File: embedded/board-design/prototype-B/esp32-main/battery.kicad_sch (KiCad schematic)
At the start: 14 parts, among them J8 Conn_01x03_Socket, Q5 FDN340P, Q6 FDN340P, U5 LTC4054ES5-4.2

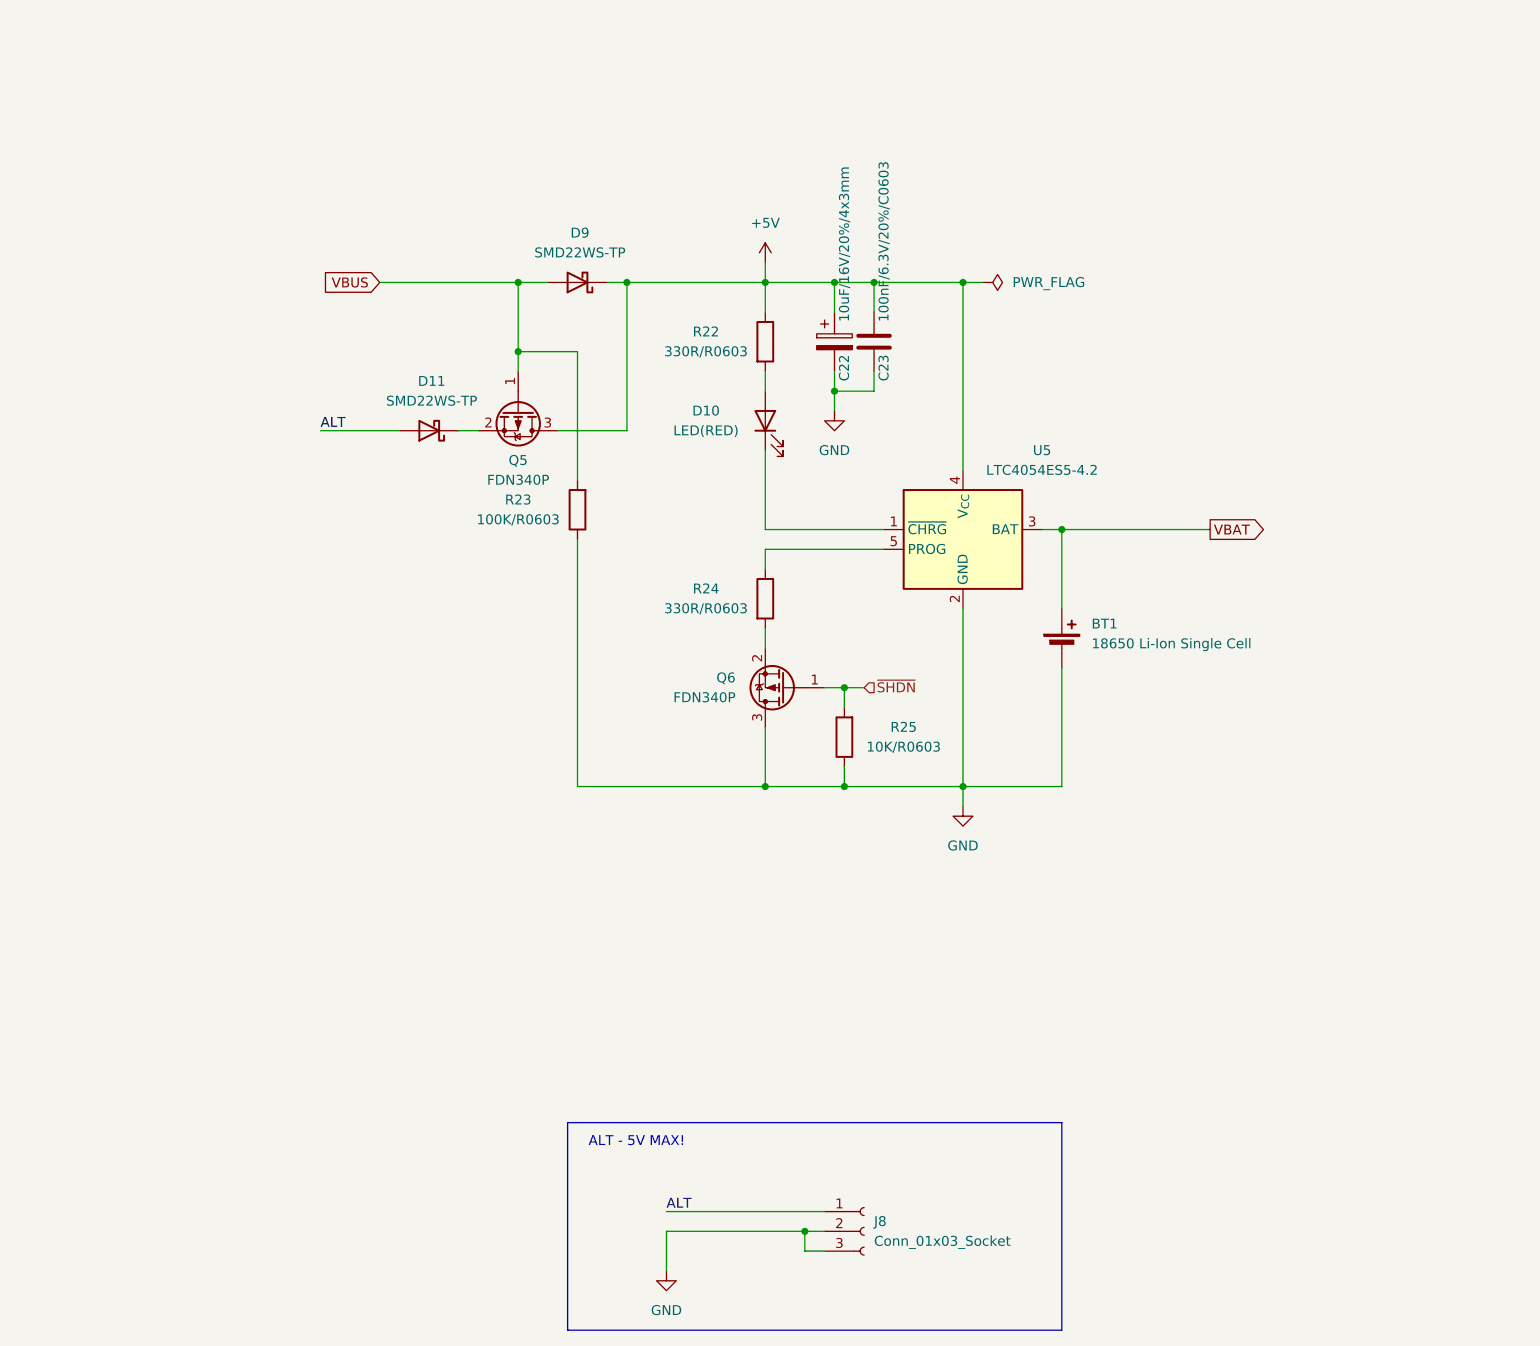
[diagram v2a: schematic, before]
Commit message: [prototype-B]
Refactored power scheme.

Signed-off-by: Nicolae-Andrei Vasile <vasilenicolaeandrei@gmail.com>
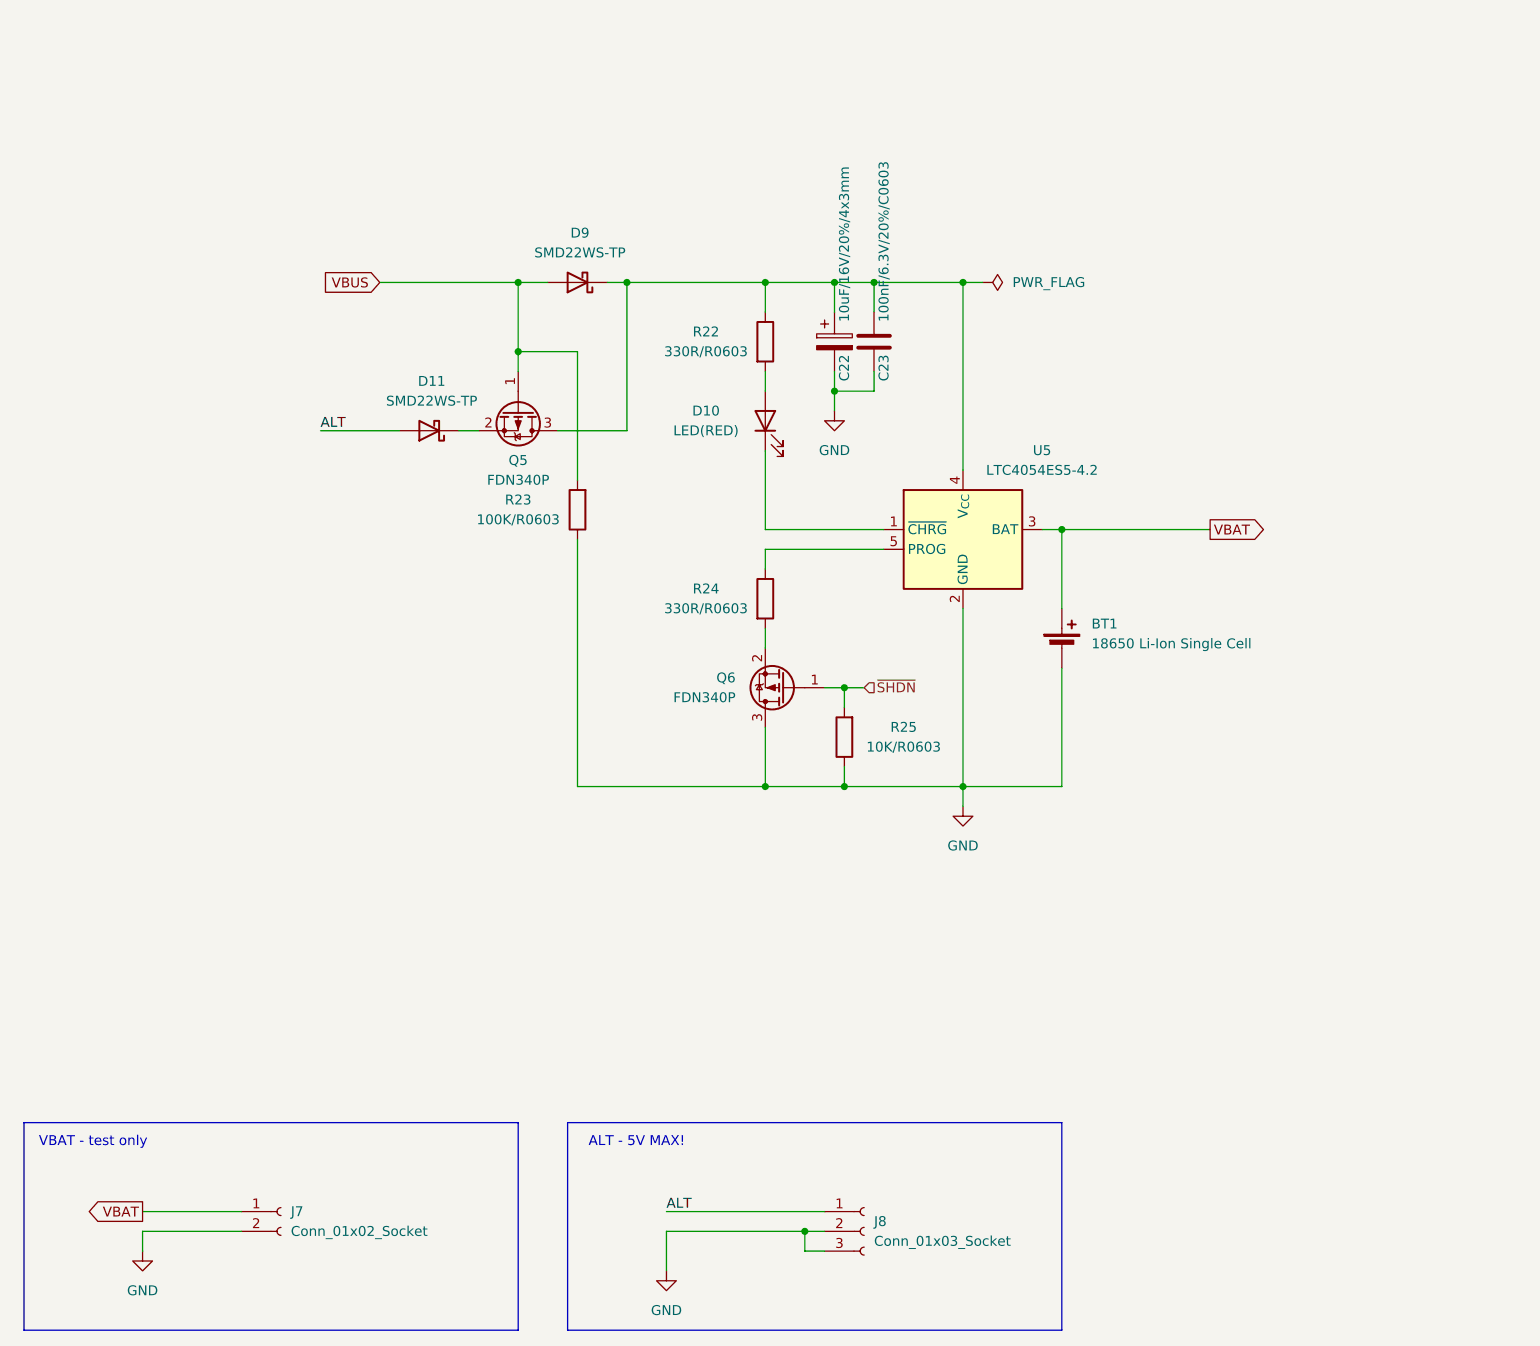
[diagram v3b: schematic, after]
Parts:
- added J7: Conn_01x02_Socket, Connector_PinHeader_1.27mm:PinHeader_1x02_P1.27mm_Vertical, symbol Connector:Conn_01x02_Socket
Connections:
- net GND: now also J7.2 (Pin_2)
- net VBAT: now also J7.1 (Pin_1)
- net +5V: no longer names the net of C22.1, C23.1, D9.1 (K), Q5.3 (D), R22.1, U5.4 (V_{CC})
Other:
- note added: "VBAT - test only"
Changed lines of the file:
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@@
+		)
+	)
+	(polyline
+		(pts
+			(xy 101.6 193.04) (xy 101.6 166.37)
+		)
+		(stroke
+			(width 0)
+			(type default)
 		)
 	)
@@
 	(polyline
 		(pts
+			(xy 38.1 193.04) (xy 101.6 193.04)
+		)
+		(stroke
+			(width 0)
+			(type default)
+		)
+	)
+	(polyline
+		(pts
 			(xy 171.45 193.04) (xy 171.45 166.37)
 		)
@@
 		)
 	)
+	(polyline
+		(pts
+			(xy 38.1 166.37) (xy 38.1 193.04)
+		)
+		(stroke
+			(width 0)
+			(type default)
+		)
+	)
 	(wire
 		(pts
@@
 	(wire
 		(pts
-			(xy 133.35 55.88) (xy 133.35 58.42)
+			(xy 66.04 180.34) (xy 53.34 180.34)
 		)
 		(stroke
@@
 	(wire
 		(pts
+			(xy 53.34 177.8) (xy 66.04 177.8)
+		)
+		(stroke
+			(width 0)
+			(type default)
+		)
+	)
+	(wire
+		(pts
 			(xy 109.22 67.31) (xy 101.6 67.31)
 		)
@@
 	(wire
 		(pts
+			(xy 53.34 180.34) (xy 53.34 182.88)
+		)
+		(stroke
+			(width 0)
+			(type default)
+		)
+	)
+	(wire
+		(pts
 			(xy 147.32 72.39) (xy 147.32 69.85)
 		)
@@
 		)
 	)
+	(polyline
+		(pts
+			(xy 101.6 166.37) (xy 38.1 166.37)
+		)
+		(stroke
+			(width 0)
+			(type default)
+		)
+	)
 	(wire
 		(pts
@@
 			(width 0)
 			(type default)
+		)
+	)
+	(text "VBAT - test only"
+		(exclude_from_sim no)
+		(at 46.99 168.91 0)
+		(effects
+			(font
+				(size 1.27 1.27)
+			)
 		)
 	)
@@
 		(property "Intersheetrefs" "${INTERSHEET_REFS}"
 			(at 75.9362 58.42 0)
+			(effects
+				(font
+					(size 1.27 1.27)
+				)
+				(justify right)
+				(hide yes)
+			)
+		)
+	)
+	(global_label "VBAT"
+		(shape output)
+		(at 53.34 177.8 180)
+		(fields_autoplaced yes)
+		(effects
+			(font
+				(size 1.27 1.27)
+			)
+			(justify right)
+		)
+		(property "Intersheetrefs" "${INTERSHEET_REFS}"
+			(at 45.94 177.8 0)
 			(effects
 				(font
@@
 	)
 	(symbol
-		(lib_id "power:+5V")
-		(at 133.35 55.88 0)
-		(unit 1)
-		(exclude_from_sim no)
-		(in_bom yes)
-		(on_board yes)
-		(dnp no)
-		(fields_autoplaced yes)
-		(property "Reference" "#PWR024"
-			(at 133.35 59.69 0)
-			(effects
-				(font
-					(size 1.27 1.27)
-				)
-				(hide yes)
-			)
-		)
-		(property "Value" "+5V"
-			(at 133.35 50.8 0)
-			(effects
-				(font
-					(size 1.27 1.27)
-				)
-			)
-		)
-		(property "Footprint" ""
-			(at 133.35 55.88 0)
-			(effects
-				(font
-					(size 1.27 1.27)
-				)
-				(hide yes)
-			)
-		)
-		(property "Datasheet" ""
-			(at 133.35 55.88 0)
-			(effects
-				(font
-					(size 1.27 1.27)
-				)
-				(hide yes)
-			)
-		)
-		(property "Description" "Power symbol creates a global label with name \"+5V\""
-			(at 133.35 55.88 0)
-			(effects
-				(font
-					(size 1.27 1.27)
-				)
-				(hide yes)
-			)
-		)
-		(pin "1"
-		)
-		(instances
-			(project ""
-				(path "/6d02e045-d1b3-4320-a4f8-f5e2c734acd4/9cfdfa29-fef4-49c3-96a5-094ec94d9453"
-					(reference "#PWR024")
-					(unit 1)
-				)
-			)
-		)
-	)
-	(symbol
 		(lib_id "power:GND")
 		(at 158.75 125.73 0)
@@
 					(unit 1)
 				)
+			)
+		)
+	)
+	(symbol
+		(lib_id "power:GND")
+		(at 53.34 182.88 0)
+		(unit 1)
+		(exclude_from_sim no)
+		(in_bom yes)
+		(on_board yes)
+		(dnp no)
+		(fields_autoplaced yes)
+		(property "Reference" "#PWR023"
+			(at 53.34 189.23 0)
+			(effects
+				(font
+					(size 1.27 1.27)
+				)
+				(hide yes)
+			)
+		)
+		(property "Value" "GND"
+			(at 53.34 187.96 0)
+			(effects
+				(font
+					(size 1.27 1.27)
+				)
+			)
+		)
+		(property "Footprint" ""
+			(at 53.34 182.88 0)
+			(effects
+				(font
+					(size 1.27 1.27)
+				)
+				(hide yes)
+			)
+		)
+		(property "Datasheet" ""
+			(at 53.34 182.88 0)
+			(effects
+				(font
+					(size 1.27 1.27)
+				)
+				(hide yes)
+			)
+		)
+		(property "Description" "Power symbol creates a global label with name \"GND\" , ground"
+			(at 53.34 182.88 0)
+			(effects
+				(font
+					(size 1.27 1.27)
+				)
+				(hide yes)
+			)
+		)
+		(pin "1"
+		)
+		(instances
+			(project "esp32-main"
+				(path "/6d02e045-d1b3-4320-a4f8-f5e2c734acd4/9cfdfa29-fef4-49c3-96a5-094ec94d9453"
+					(reference "#PWR023")
+					(unit 1)
+				)
+			)
+		)
+	)
+	(symbol
+		(lib_id "Connector:Conn_01x02_Socket")
+		(at 71.12 177.8 0)
+		(unit 1)
+		(exclude_from_sim no)
+		(in_bom yes)
+		(on_board yes)
+		(dnp no)
+		(fields_autoplaced yes)
+		(property "Reference" "J7"
+			(at 72.39 177.7999 0)
+			(effects
+				(font
+					(size 1.27 1.27)
+				)
+				(justify left)
+			)
+		)
+		(property "Value" "Conn_01x02_Socket"
+			(at 72.39 180.3399 0)
+			(effects
+				(font
+					(size 1.27 1.27)
+				)
+				(justify left)
+			)
+		)
+		(property "Footprint" "Connector_PinHeader_1.27mm:PinHeader_1x02_P1.27mm_Vertical"
+			(at 71.12 177.8 0)
+			(effects
+				(font
+					(size 1.27 1.27)
+				)
+				(hide yes)
+			)
+		)
+		(property "Datasheet" "~"
+			(at 71.12 177.8 0)
+			(effects
+				(font
+					(size 1.27 1.27)
+				)
+				(hide yes)
+			)
+		)
+		(property "Description" "Generic connector, single row, 01x02, script generated"
+			(at 71.12 177.8 0)
+			(effects
+				(font
+					(size 1.27 1.27)
+				)
+				(hide yes)
+			)
+		)
+		(pin "1"
+		)
+		(pin "2"
+		)
+		(instances
+			(project "esp32-main"
+				(path "/6d02e045-d1b3-4320-a4f8-f5e2c734acd4/9cfdfa29-fef4-49c3-96a5-094ec94d9453"
+					(reference "J7")
+					(unit 1)
+				)
